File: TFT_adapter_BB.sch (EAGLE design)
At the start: 3 parts

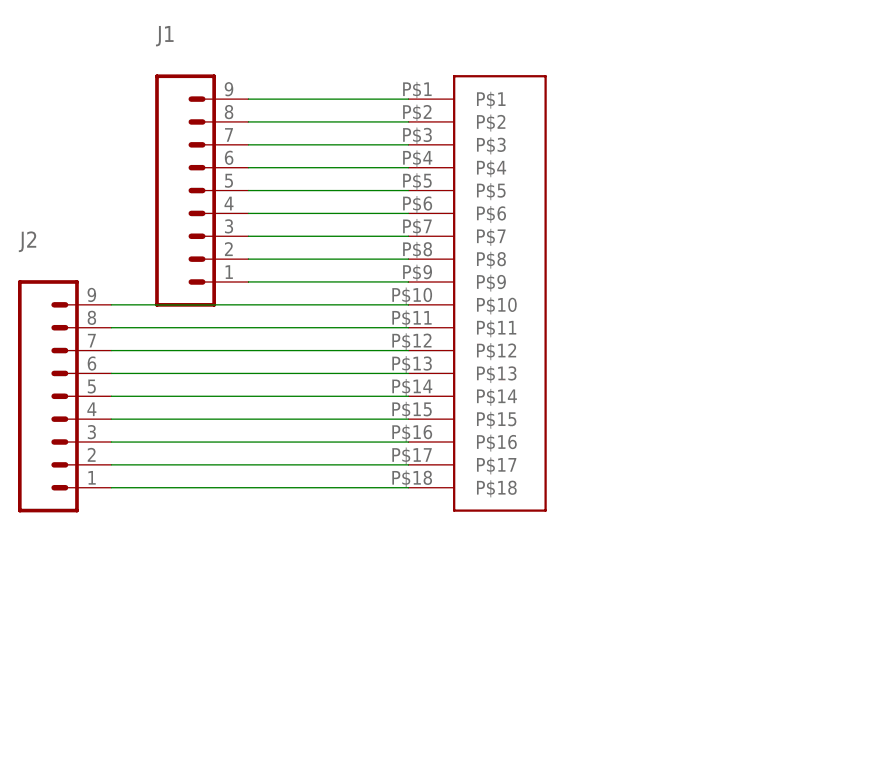
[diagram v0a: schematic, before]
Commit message: Added the breadboard TFT adapater
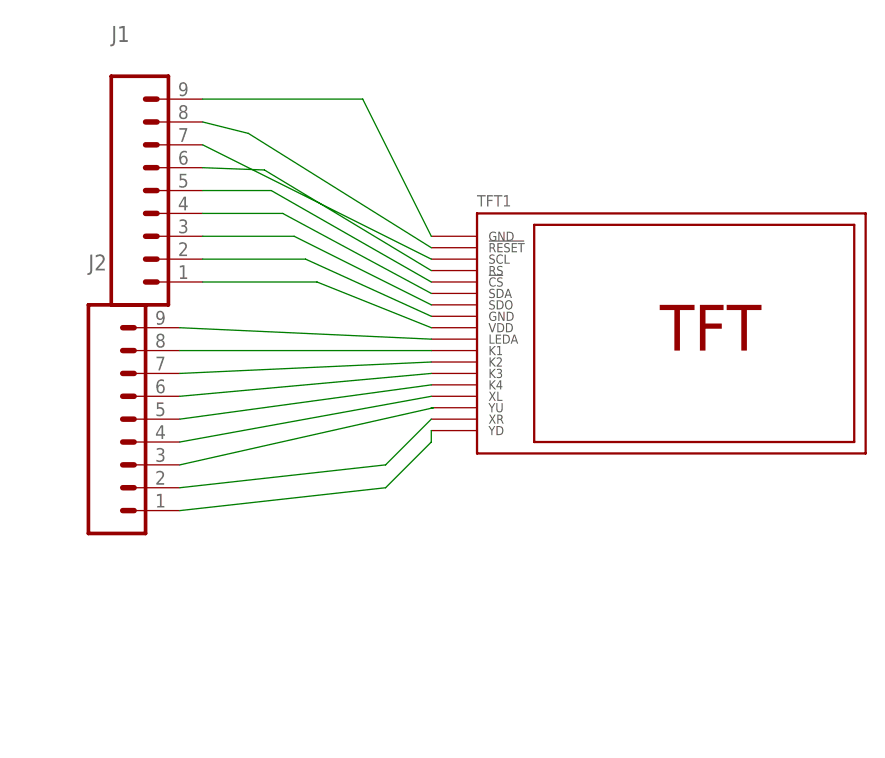
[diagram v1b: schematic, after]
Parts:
- removed U$2: FCC-18-0.8MM, custom:FCC-18-0.8MM
- added TFT1: TFT-18-1.0MM, custom:TFT-18-1.0MM
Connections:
- removed net N$1: J1.9, U$2.P$1
- removed net N$18: J2.1, U$2.P$18
- removed net N$7: J1.3, U$2.P$7
- removed net N$8: J1.2, U$2.P$8
- removed net N$9: J1.1, U$2.P$9
- new net GND: J1.3, J1.9, TFT1.GND@1, TFT1.SDO
- new net GND2: J1.2, TFT1.GND@2
- new net LEDA: J2.9, TFT1.LEDA
- new net VDD: J1.1, TFT1.VDD
- net N$10: now also J2.1, TFT1.YD; no longer J2.9, U$2.P$10
- net N$11: now also J2.2, TFT1.XR; no longer J2.8, U$2.P$11
- net N$12: now also J2.3, TFT1.YU; no longer J2.7, U$2.P$12
- net N$13: now also J2.4, TFT1.XL; no longer J2.6, U$2.P$13
- net N$14: now also TFT1.K4; no longer U$2.P$14
- net N$15: now also J2.7, TFT1.K2; no longer J2.4, U$2.P$15
- net N$16: now also J2.6, TFT1.K3; no longer J2.3, U$2.P$16
- net N$17: now also J2.8, TFT1.K1; no longer J2.2, U$2.P$17
- net N$2: now also TFT1.!RESET; no longer U$2.P$2
- net N$3: now also TFT1.SCL; no longer U$2.P$3
- net N$4: now also TFT1.RS; no longer U$2.P$4
- net N$5: now also TFT1.!CS; no longer U$2.P$5
- net N$6: now also TFT1.SDA; no longer U$2.P$6
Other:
- moved on the sheet: J1, J2

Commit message: Finished the coprocessor
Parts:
- added U$1: CBT3244AD, custom:CBT3244AD
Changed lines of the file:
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@@
 <setting verticaltext="up"/>
 </settings>
-<grid distance="0.1" unitdist="inch" unit="inch" style="lines" multiple="1" display="no" altdistance="0.05" altunitdist="inch" altunit="inch"/>
+<grid distance="0.1" unitdist="inch" unit="inch" style="lines" multiple="1" display="no" altdistance="0.01" altunitdist="inch" altunit="inch"/>
 <layers>
 <layer number="1" name="Top" color="4" fill="1" visible="no" active="no"/>
@@
 <part name="J2" library="SparkFun-Connectors" deviceset="M09" device="NO_SILK"/>
 <part name="TFT1" library="custom" deviceset="TFT-18-1.0MM" device=""/>
+<part name="U$1" library="custom" deviceset="CBT3244AD" device=""/>
 </parts>
 <sheets>
@@
 <instance part="J2" gate="G$1" x="-7.62" y="2.54"/>
 <instance part="TFT1" gate="TFT$1" x="35.56" y="22.86"/>
+<instance part="U$1" gate="G$1" x="43.18" y="-17.78"/>
 </instances>
 <busses>
